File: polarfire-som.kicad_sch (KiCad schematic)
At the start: 17 parts, among them J2 Tag-Connect_TC2030-IDC-NL_2x3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, U1 MPFS250T-FCVG484

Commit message: [#57505] Continue migration to hierarchical schematic
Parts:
- removed J2: Tag-Connect_TC2030-IDC-NL_2x3_P1.27mm, antmicro-footprints:Tag-Connect_TC2030-IDC-NL_2x3_P1.27mm, symbol antmicroTestPoints:Tag-Connect_TC2030-IDC-NL_2x3_P1.27mm
- removed R154, R42: R_1k_0402, antmicro-footprints:R_0402_1005Metric, symbol antmicroResistors0402:R_1k_0402
- removed R155: R_10k_0402, antmicro-footprints:R_0402_1005Metric, symbol antmicroResistors0402:R_10k_0402
- removed R39, R40, R41: R_4k7_0402, antmicro-footprints:R_0402_1005Metric, symbol antmicroResistors0402:R_4k7_0402
- removed R43, R44: R_0R_0402, antmicro-footprints:R_0402_1005Metric, symbol antmicroResistors0402:R_0R_0402
- removed TP1: TP_0.75mm_SMD, antmicro-footprints:TP_SMD_0.75mm, symbol antmicroTestPoints:TP_0.75mm_SMD
- removed U1: MPFS250T-FCVG484, antmicro-footprints:BGA-484_19x19mm_Layout22x22_P0.8mm-microchip-technology-mpfs250t-fcvg484, symbol antmicroFPGAChips:MPFS250T-FCVG484
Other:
- sheet Misc renamed Memory
- removed sheet Connectors
- added sheet FPGA Config (fpga-config.kicad_sch)
- sheet FPGA GPIO ports: added HDMI_FPGA{HDMI}, WiFi{SDIO}; removed none
- sheet FPGA HSIO ports: added Crosslink_B1{subLVDS}, Crosslink_B2{subLVDS}; removed none
- sheet FPGA MSSIO ports: added ID{I^{2}C}, SUPPLY{I^{2}C}; removed none
- sheet HDMI ports: added HDMI_FPGA{HDMI}; removed none
- sheet MIPI CrossLink ports: added Crosslink_B1{subLVDS}, Crosslink_B2{subLVDS}; removed none
- sheet Memory: file misc.kicad_sch -> memory.kicad_sch
- sheet WiFi_Bluetooth ports: added WiFi{SDIO}; removed none
- note added: "MPFS250T FCVG484"
- note added: "User LED"
- note removed: "JTAG"
- note removed: "PolarFire Bank 3 JTAG/DEDIO"

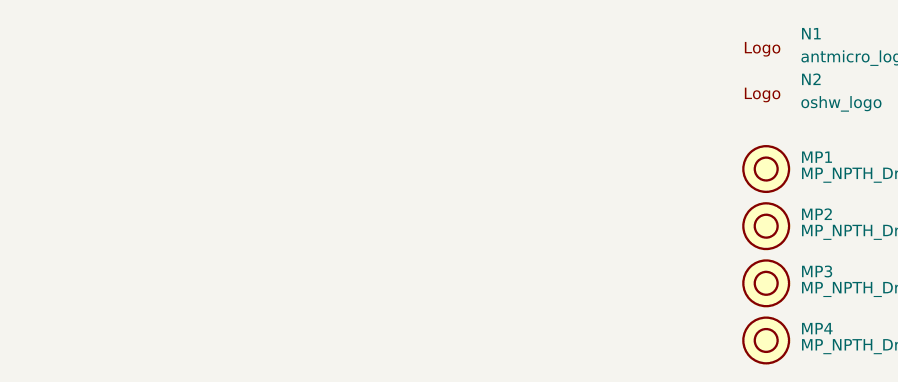
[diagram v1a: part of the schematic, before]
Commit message: [#57422] Add ETH PHY strap, WL_BT UART level shifter, fiducials, remove BYP_EN
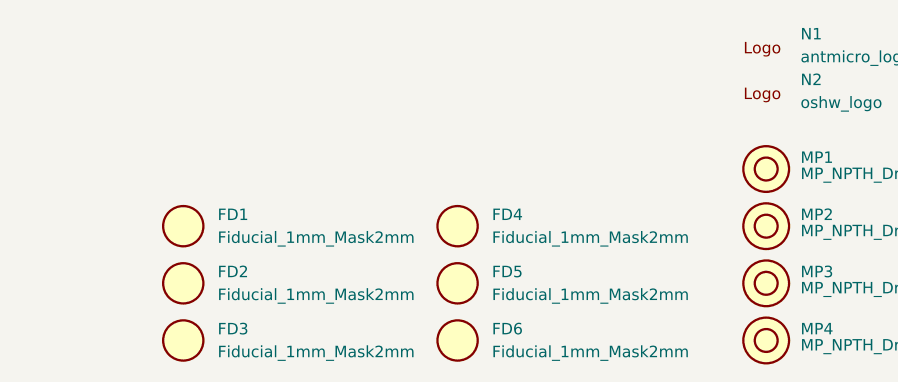
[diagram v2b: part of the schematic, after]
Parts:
- added FD1, FD2, FD3, FD4, FD5, FD6: Fiducial_1mm_Mask2mm, antmicro-footprints:Fiducial_1mm_Mask2mm, symbol antmicroFiducialMarks:Fiducial_1mm_Mask2mm
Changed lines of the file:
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@@
     (effects (font (size 1.27 1.27)) (justify left bottom))
+  )
+  (symbol (lib_id "antmicroFiducialMarks:Fiducial_1mm_Mask2mm") (at 308.61 242.57 0) (unit 1)
+    (in_bom no) (on_board yes) (dnp no) (fields_autoplaced)
+    (property "Reference" "FD3" (at 312.42 241.3 0)
+      (effects (font (size 1.27 1.27) (thickness 0.15)) (justify left))
+    )
+    (property "Value" "Fiducial_1mm_Mask2mm" (at 312.42 243.84 0)
+      (effects (font (size 1.27 1.27) (thickness 0.15)) (justify left))
+    )
+    (property "Footprint" "antmicro-footprints:Fiducial_1mm_Mask2mm" (at 317.5 247.65 0)
+      (effects (font (size 1.27 1.27) (thickness 0.15)) (justify left bottom) hide)
+    )
+    (property "Datasheet" "" (at 317.83 253.06 0)
+      (effects (font (size 1.27 1.27) (thickness 0.15)) (justify left bottom) hide)
+    )
+    (property "Author" "Antmicro" (at 317.83 249.885 0)
+      (effects (font (size 1.27 1.27) (thickness 0.15)) (justify left bottom) hide)
+    )
+    (property "License" "Apache-2.0" (at 317.83 252.425 0)
+      (effects (font (size 1.27 1.27) (thickness 0.15)) (justify left bottom) hide)
+    )
+    (instances
+      (project "polarfire-som"
+        (path "/db4a0d3e-2eb3-499e-977d-6eb378cfd3ed"
+          (reference "FD3") (unit 1)
+        )
+      )
+    )
+  )
+  (symbol (lib_id "antmicroFiducialMarks:Fiducial_1mm_Mask2mm") (at 308.61 236.22 0) (unit 1)
+    (in_bom no) (on_board yes) (dnp no) (fields_autoplaced)
+    (property "Reference" "FD2" (at 312.42 234.95 0)
+      (effects (font (size 1.27 1.27) (thickness 0.15)) (justify left))
+    )
+    (property "Value" "Fiducial_1mm_Mask2mm" (at 312.42 237.49 0)
+      (effects (font (size 1.27 1.27) (thickness 0.15)) (justify left))
+    )
+    (property "Footprint" "antmicro-footprints:Fiducial_1mm_Mask2mm" (at 317.5 241.3 0)
+      (effects (font (size 1.27 1.27) (thickness 0.15)) (justify left bottom) hide)
+    )
+    (property "Datasheet" "" (at 317.83 246.71 0)
+      (effects (font (size 1.27 1.27) (thickness 0.15)) (justify left bottom) hide)
+    )
+    (property "Author" "Antmicro" (at 317.83 243.535 0)
+      (effects (font (size 1.27 1.27) (thickness 0.15)) (justify left bottom) hide)
+    )
+    (property "License" "Apache-2.0" (at 317.83 246.075 0)
+      (effects (font (size 1.27 1.27) (thickness 0.15)) (justify left bottom) hide)
+    )
+    (instances
+      (project "polarfire-som"
+        (path "/db4a0d3e-2eb3-499e-977d-6eb378cfd3ed"
+          (reference "FD2") (unit 1)
+        )
+      )
+    )
   )
   (symbol (lib_id "antmicroMechanicalParts:MP_NPTH_Drill2.7mm") (at 373.38 223.52 0) (unit 1)
@@
     )
   )
+  (symbol (lib_id "antmicroFiducialMarks:Fiducial_1mm_Mask2mm") (at 339.09 229.87 0) (unit 1)
+    (in_bom no) (on_board yes) (dnp no) (fields_autoplaced)
+    (property "Reference" "FD4" (at 342.9 228.6 0)
+      (effects (font (size 1.27 1.27) (thickness 0.15)) (justify left))
+    )
+    (property "Value" "Fiducial_1mm_Mask2mm" (at 342.9 231.14 0)
+      (effects (font (size 1.27 1.27) (thickness 0.15)) (justify left))
+    )
+    (property "Footprint" "antmicro-footprints:Fiducial_1mm_Mask2mm" (at 347.98 234.95 0)
+      (effects (font (size 1.27 1.27) (thickness 0.15)) (justify left bottom) hide)
+    )
+    (property "Datasheet" "" (at 348.31 240.36 0)
+      (effects (font (size 1.27 1.27) (thickness 0.15)) (justify left bottom) hide)
+    )
+    (property "Author" "Antmicro" (at 348.31 237.185 0)
+      (effects (font (size 1.27 1.27) (thickness 0.15)) (justify left bottom) hide)
+    )
+    (property "License" "Apache-2.0" (at 348.31 239.725 0)
+      (effects (font (size 1.27 1.27) (thickness 0.15)) (justify left bottom) hide)
+    )
+    (instances
+      (project "polarfire-som"
+        (path "/db4a0d3e-2eb3-499e-977d-6eb378cfd3ed"
+          (reference "FD4") (unit 1)
+        )
+      )
+    )
+  )
+  (symbol (lib_id "antmicroFiducialMarks:Fiducial_1mm_Mask2mm") (at 308.61 229.87 0) (unit 1)
+    (in_bom no) (on_board yes) (dnp no) (fields_autoplaced)
+    (property "Reference" "FD1" (at 312.42 228.6 0)
+      (effects (font (size 1.27 1.27) (thickness 0.15)) (justify left))
+    )
+    (property "Value" "Fiducial_1mm_Mask2mm" (at 312.42 231.14 0)
+      (effects (font (size 1.27 1.27) (thickness 0.15)) (justify left))
+    )
+    (property "Footprint" "antmicro-footprints:Fiducial_1mm_Mask2mm" (at 317.5 234.95 0)
+      (effects (font (size 1.27 1.27) (thickness 0.15)) (justify left bottom) hide)
+    )
+    (property "Datasheet" "" (at 317.83 240.36 0)
+      (effects (font (size 1.27 1.27) (thickness 0.15)) (justify left bottom) hide)
+    )
+    (property "Author" "Antmicro" (at 317.83 237.185 0)
+      (effects (font (size 1.27 1.27) (thickness 0.15)) (justify left bottom) hide)
+    )
+    (property "License" "Apache-2.0" (at 317.83 239.725 0)
+      (effects (font (size 1.27 1.27) (thickness 0.15)) (justify left bottom) hide)
+    )
+    (instances
+      (project "polarfire-som"
+        (path "/db4a0d3e-2eb3-499e-977d-6eb378cfd3ed"
+          (reference "FD1") (unit 1)
+        )
+      )
+    )
+  )
   (symbol (lib_id "antmicroMechanicalParts:MP_NPTH_Drill2.7mm") (at 373.38 229.87 0) (unit 1)
     (in_bom no) (on_board yes) (dnp no)
@@
         )
       )
+    )
+  )
+  (symbol (lib_id "antmicroFiducialMarks:Fiducial_1mm_Mask2mm") (at 339.09 236.22 0) (unit 1)
+    (in_bom no) (on_board yes) (dnp no) (fields_autoplaced)
+    (property "Reference" "FD5" (at 342.9 234.95 0)
+      (effects (font (size 1.27 1.27) (thickness 0.15)) (justify left))
+    )
+    (property "Value" "Fiducial_1mm_Mask2mm" (at 342.9 237.49 0)
+      (effects (font (size 1.27 1.27) (thickness 0.15)) (justify left))
+    )
+    (property "Footprint" "antmicro-footprints:Fiducial_1mm_Mask2mm" (at 347.98 241.3 0)
+      (effects (font (size 1.27 1.27) (thickness 0.15)) (justify left bottom) hide)
+    )
+    (property "Datasheet" "" (at 348.31 246.71 0)
+      (effects (font (size 1.27 1.27) (thickness 0.15)) (justify left bottom) hide)
+    )
+    (property "Author" "Antmicro" (at 348.31 243.535 0)
+      (effects (font (size 1.27 1.27) (thickness 0.15)) (justify left bottom) hide)
+    )
+    (property "License" "Apache-2.0" (at 348.31 246.075 0)
+      (effects (font (size 1.27 1.27) (thickness 0.15)) (justify left bottom) hide)
+    )
+    (instances
+      (project "polarfire-som"
+        (path "/db4a0d3e-2eb3-499e-977d-6eb378cfd3ed"
+          (reference "FD5") (unit 1)
+        )
+      )
+    )
+  )
+  (symbol (lib_id "antmicroFiducialMarks:Fiducial_1mm_Mask2mm") (at 339.09 242.57 0) (unit 1)
+    (in_bom no) (on_board yes) (dnp no) (fields_autoplaced)
+    (property "Reference" "FD6" (at 342.9 241.3 0)
+      (effects (font (size 1.27 1.27) (thickness 0.15)) (justify left))
+    )
+    (property "Value" "Fiducial_1mm_Mask2mm" (at 342.9 243.84 0)
+      (effects (font (size 1.27 1.27) (thickness 0.15)) (justify left))
+    )
+    (property "Footprint" "antmicro-footprints:Fiducial_1mm_Mask2mm" (at 347.98 247.65 0)
+      (effects (font (size 1.27 1.27) (thickness 0.15)) (justify left bottom) hide)
+    )
+    (property "Datasheet" "" (at 348.31 253.06 0)
+      (effects (font (size 1.27 1.27) (thickness 0.15)) (justify left bottom) hide)
+    )
+    (property "Author" "Antmicro" (at 348.31 249.885 0)
+      (effects (font (size 1.27 1.27) (thickness 0.15)) (justify left bottom) hide)
+    )
+    (property "License" "Apache-2.0" (at 348.31 252.425 0)
+      (effects (font (size 1.27 1.27) (thickness 0.15)) (justify left bottom) hide)
+    )
+    (instances
+      (project "polarfire-som"
+        (path "/db4a0d3e-2eb3-499e-977d-6eb378cfd3ed"
+          (reference "FD6") (unit 1)
+        )
+      )

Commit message: [#57505] Finish defining buses
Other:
- sheet Bottom Connector ports: added CONN{USB}; removed none
- sheet FPGA MSSIO ports: added PF_BT{UART}; removed MEM{SDIO}
- sheet Supply ports: added SUPPLY{I^{2}C}; removed none
- sheet Top Connector ports: added ID{I^{2}C}; removed none
- sheet USB ports: added CONN{USB}, WL_BT{USB}; removed none
- sheet WiFi_Bluetooth ports: added PF_BT{UART}, WL_BT{USB}; removed none
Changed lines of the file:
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@@
+    (stroke (width 0) (type default))
+  )
+  (bus (pts (xy 262.89 106.68) (xy 265.43 106.68))
     (stroke (width 0) (type default))
   )
@@
     (stroke (width 0) (type default))
   )
+  (bus (pts (xy 278.765 70.485) (xy 278.765 109.22))
+    (stroke (width 0) (type default))
+  )
   (bus (pts (xy 165.735 165.735) (xy 273.685 165.735))
     (stroke (width 0) (type default))
   )
+  (bus (pts (xy 311.15 140.335) (xy 311.15 161.925))
+    (stroke (width 0) (type default))
+  )
   (polyline (pts (xy 266.7 84.455) (xy 266.7 163.83))
     (stroke (width 0) (type default))
@@
     (stroke (width 0) (type default))
   )
+  (bus (pts (xy 265.43 106.68) (xy 265.43 113.665))
+    (stroke (width 0) (type default))
+  )
   (bus (pts (xy 201.93 157.48) (xy 203.835 157.48))
     (stroke (width 0) (type default))
@@
     (stroke (width 0) (type default))
   )
+  (bus (pts (xy 262.89 100.965) (xy 274.955 100.965))
+    (stroke (width 0) (type default))
+  )
   (bus (pts (xy 161.925 170.815) (xy 161.925 147.955))
     (stroke (width 0) (type default))
@@
     (stroke (width 0) (type default))
   )
+  (bus (pts (xy 311.15 161.925) (xy 307.975 161.925))
+    (stroke (width 0) (type default))
+  )
+  (bus (pts (xy 274.955 164.465) (xy 281.305 164.465))
+    (stroke (width 0) (type default))
+  )
+  (bus (pts (xy 307.975 140.335) (xy 311.15 140.335))
+    (stroke (width 0) (type default))
+  )
   (bus (pts (xy 312.42 75.565) (xy 312.42 89.535))
     (stroke (width 0) (type default))
   )
+  (bus (pts (xy 274.955 100.965) (xy 274.955 164.465))
+    (stroke (width 0) (type default))
+  )
+  (bus (pts (xy 262.255 70.485) (xy 278.765 70.485))
+    (stroke (width 0) (type default))
+  )
   (bus (pts (xy 163.83 142.875) (xy 172.72 142.875))
     (stroke (width 0) (type default))
   )
+  (bus (pts (xy 265.43 113.665) (xy 164.465 113.665))
+    (stroke (width 0) (type default))
+  )
   (bus (pts (xy 172.72 145.415) (xy 165.735 145.415))
     (stroke (width 0) (type default))
@@
     (stroke (width 0) (type default))
   )
+  (bus (pts (xy 314.96 204.47) (xy 314.96 137.795))
+    (stroke (width 0) (type default))
+  )
+  (bus (pts (xy 164.465 113.665) (xy 164.465 129.54))
+    (stroke (width 0) (type default))
+  )
   (bus (pts (xy 273.685 165.735) (xy 273.685 161.925))
     (stroke (width 0) (type default))
@@
     (stroke (width 0) (type default))
   )
+  (bus (pts (xy 164.465 129.54) (xy 154.94 129.54))
+    (stroke (width 0) (type default))
+  )
   (bus (pts (xy 201.93 157.48) (xy 201.93 191.77))
     (stroke (width 0) (type default))
@@
     (stroke (width 0) (type default))
   )
+  (bus (pts (xy 261.62 204.47) (xy 314.96 204.47))
+    (stroke (width 0) (type default))
+  )
+  (bus (pts (xy 314.96 137.795) (xy 307.975 137.795))
+    (stroke (width 0) (type default))
+  )
   (bus (pts (xy 222.885 81.28) (xy 273.05 81.28))
     (stroke (width 0) (type default))
   )
   (bus (pts (xy 271.145 173.99) (xy 262.255 173.99))
+    (stroke (width 0) (type default))
+  )
+  (bus (pts (xy 278.765 109.22) (xy 262.89 109.22))
     (stroke (width 0) (type default))
   )
@@
       (effects (font (size 1.27 1.27)) (justify left))
     )
+    (pin "WL_BT{USB}" input (at 307.975 161.925 0)
+      (effects (font (size 1.27 1.27)) (justify right))
+    )
+    (pin "PF_BT{UART}" input (at 281.305 164.465 180)
+      (effects (font (size 1.27 1.27)) (justify left))
+    )
     (instances
       (project "polarfire-som"
@@
     )
   )
-  (sheet (at 172.72 116.205) (size 26.67 17.78) (fields_autoplaced)
+  (sheet (at 172.847 116.967) (size 26.67 17.78) (fields_autoplaced)
     (stroke (width 0.1524) (type solid))
     (fill (color 0 0 0 0.0000))
-    (property "Sheetname" "FPGA Supply" (at 172.72 115.4934 0)
+    (property "Sheetname" "FPGA Supply" (at 172.847 116.2554 0)
       (effects (font (size 1.27 1.27)) (justify left bottom))
     )
-    (property "Sheetfile" "fpga-supply.kicad_sch" (at 172.72 134.5696 0)
+    (property "Sheetfile" "fpga-supply.kicad_sch" (at 172.847 135.3316 0)
       (effects (font (size 1.27 1.27)) (justify left top))
     )
@@
       (effects (font (size 1.27 1.27)) (justify left top))
     )
+    (pin "SUPPLY{I^{2}C}" input (at 154.94 129.54 0)
+      (effects (font (size 1.27 1.27)) (justify right))
+    )
     (instances
       (project "polarfire-som"
@@
       (effects (font (size 1.27 1.27)) (justify right))
     )
+    (pin "CONN{USB}" input (at 261.62 204.47 0)
+      (effects (font (size 1.27 1.27)) (justify right))
+    )
     (instances
       (project "polarfire-som"
@@
       (effects (font (size 1.27 1.27)) (justify left))
     )
+    (pin "WL_BT{USB}" input (at 307.975 140.335 0)
+      (effects (font (size 1.27 1.27)) (justify right))
+    )
+    (pin "CONN{USB}" input (at 307.975 137.795 0)
+      (effects (font (size 1.27 1.27)) (justify right))
+    )
     (instances
       (project "polarfire-som"
@@
     )
   )
-  (sheet (at 236.093 116.078) (size 26.67 17.78) (fields_autoplaced)
+  (sheet (at 236.22 116.84) (size 26.67 17.78) (fields_autoplaced)
     (stroke (width 0.1524) (type solid))
     (fill (color 0 0 0 0.0000))
-    (property "Sheetname" "FPGA Config" (at 236.093 115.3664 0)
+    (property "Sheetname" "FPGA Config" (at 236.22 116.1284 0)
       (effects (font (size 1.27 1.27)) (justify left bottom))
     )
-    (property "Sheetfile" "fpga-config.kicad_sch" (at 236.093 134.4426 0)
+    (property "Sheetfile" "fpga-config.kicad_sch" (at 236.22 135.2046 0)
       (effects (font (size 1.27 1.27)) (justify left top))
     )
@@
       (effects (font (size 1.27 1.27)) (justify right))
     )
+    (pin "ID{I^{2}C}" input (at 262.255 70.485 0)
+      (effects (font (size 1.27 1.27)) (justify right))
+    )
     (instances
       (project "polarfire-som"
@@
       (effects (font (size 1.27 1.27)) (justify right))
     )
-    (pin "MEM{SDIO}" input (at 262.89 99.06 0)
-      (effects (font (size 1.27 1.27)) (justify right))
-    )
     (pin "SUPPLY{I^{2}C}" input (at 262.89 106.68 0)
       (effects (font (size 1.27 1.27)) (justify right))
@@
       (effects (font (size 1.27 1.27)) (justify right))
     )
+    (pin "PF_BT{UART}" input (at 262.89 100.965 0)
+      (effects (font (size 1.27 1.27)) (justify right))
+    )
